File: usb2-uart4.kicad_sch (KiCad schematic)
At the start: 24 parts, among them U1 CH344Q, U13 TPNUP2202W1T2G, Y1 8MHz

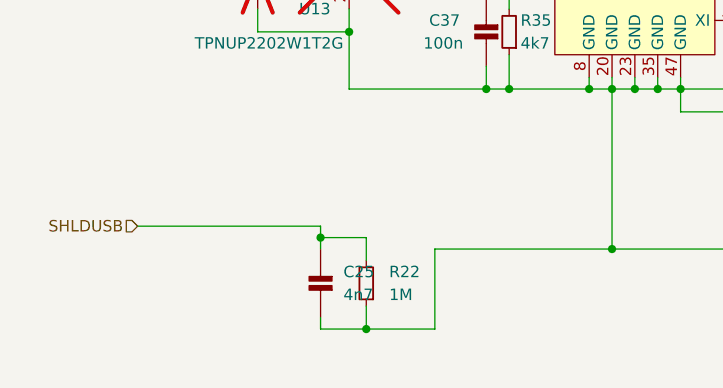
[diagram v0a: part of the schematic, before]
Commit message: Adjust R1, C1 and C10 poisitions
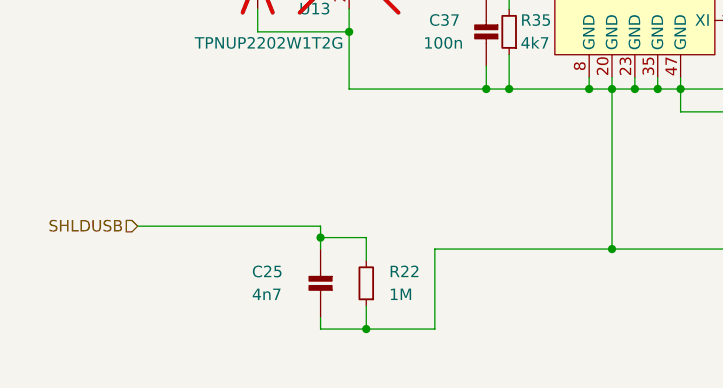
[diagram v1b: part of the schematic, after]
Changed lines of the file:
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@@
   )
   (symbol (lib_id "isouart4:CAP_NP") (at 83.82 146.05 180) (unit 1)
-    (in_bom yes) (on_board yes) (dnp no) (fields_autoplaced)
-    (property "Reference" "C25" (at 86.36 144.78 0)
+    (in_bom yes) (on_board yes) (dnp no)
+    (property "Reference" "C25" (at 76.2 144.78 0)
       (effects (font (size 1.27 1.27)) (justify right))
     )
-    (property "Value" "4n7" (at 86.36 147.32 0)
+    (property "Value" "4n7" (at 76.2 147.32 0)
       (effects (font (size 1.27 1.27)) (justify right))
     )

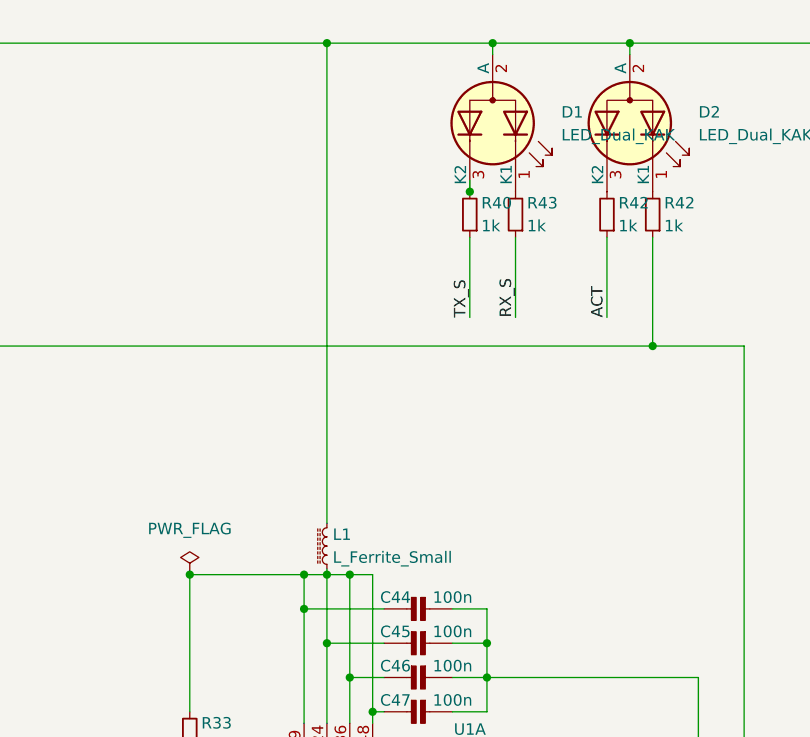
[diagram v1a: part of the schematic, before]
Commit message: adjust power filtering
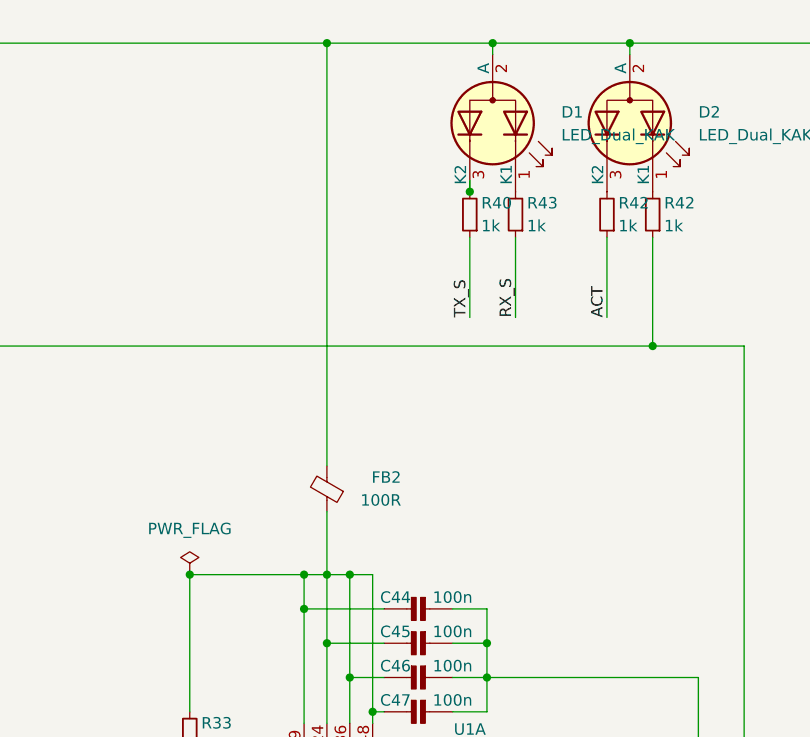
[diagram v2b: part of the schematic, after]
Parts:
- removed L1: L_Ferrite_Small, isouart4:FB_0805_2012Metric, symbol isouart4:L_Ferrite_Small
- added FB2: 100R, isouart4:FB_0805_2012Metric, symbol Device:FerriteBead_Small
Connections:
- net VIN 3.3V: now also FB2.2
- net at C44.2, C45.2, C46.2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: now also FB2.1
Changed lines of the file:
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@@
     (stroke (width 0) (type default))
   )
-  (wire (pts (xy 117.475 18.415) (xy 117.475 71.755))
+  (wire (pts (xy 117.475 18.415) (xy 117.475 65.405))
     (stroke (width 0) (type default))
   )
@@
     (stroke (width 0) (type default))
   )
-  (wire (pts (xy 117.475 76.835) (xy 117.475 77.47))
+  (wire (pts (xy 117.475 70.485) (xy 117.475 77.47))
     (stroke (width 0) (type default))
   )
@@
     )
   )
-  (symbol (lib_id "isouart4:L_Ferrite_Small") (at 117.475 74.295 180) (unit 1)
-    (in_bom yes) (on_board yes) (dnp no) (fields_autoplaced)
-    (property "Reference" "L1" (at 118.11 73.025 0)
-      (effects (font (size 1.27 1.27)) (justify right))
-    )
-    (property "Value" "L_Ferrite_Small" (at 118.11 75.565 0)
-      (effects (font (size 1.27 1.27)) (justify right))
-    )
-    (property "Footprint" "isouart4:FB_0805_2012Metric" (at 117.475 74.295 0)
-      (effects (font (size 1.27 1.27)) hide)
-    )
-    (property "Datasheet" "~" (at 117.475 74.295 0)
-      (effects (font (size 1.27 1.27)) hide)
-    )
-    (pin "1")
-    (pin "2")
-    (instances
-      (project "isouart4"
-        (path "/7c54d849-3d49-4f8e-b560-9dd1d738085c"
-          (reference "L1") (unit 1)
-        )
-        (path "/7c54d849-3d49-4f8e-b560-9dd1d738085c/2d235b8c-e233-4472-a8af-47eb53407ee3"
-          (reference "L3") (unit 1)
-        )
-      )
-    )
-  )
   (symbol (lib_id "isouart4:CAP_NP") (at 76.835 111.76 180) (unit 1)
     (in_bom no) (on_board no) (dnp yes) (fields_autoplaced)
@@
         )
       )
+    )
+  )
+  (symbol (lib_id "Device:FerriteBead_Small") (at 117.475 67.945 180) (unit 1)
+    (in_bom yes) (on_board yes) (dnp no)
+    (property "Reference" "FB2" (at 125.73 66.675 0)
+      (effects (font (size 1.27 1.27)) (justify left))
+    )
+    (property "Value" "100R" (at 125.73 69.215 0)
+      (effects (font (size 1.27 1.27)) (justify left))
+    )
+    (property "Footprint" "isouart4:FB_0805_2012Metric" (at 119.253 67.945 90)
+      (effects (font (size 1.27 1.27)) hide)
+    )
+    (property "Datasheet" "~" (at 117.475 67.945 0)
+      (effects (font (size 1.27 1.27)) hide)
+    )
+    (pin "2")
+    (pin "1")
+    (instances
+      (project "isouart4"
+        (path "/7c54d849-3d49-4f8e-b560-9dd1d738085c"
+          (reference "FB2") (unit 1)
+        )
+        (path "/7c54d849-3d49-4f8e-b560-9dd1d738085c/2d235b8c-e233-4472-a8af-47eb53407ee3"
+          (reference "FB3") (unit 1)
+        )
+      )

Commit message: Add some title text to the schematic sheets
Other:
- note added: "USB-UART"
- title: (none) -> Galvanically Isolated USB attached Quad UART
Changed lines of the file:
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@@
 (kicad_sch (version 20230121) (generator eeschema)
   (paper "A4")
+  (title_block
+    (title "Galvanically Isolated USB attached Quad UART")
+  )
   (junction (at 118.745 124.46) (diameter 0) (color 0 0 0 0)
   )
@@
     (stroke (width 0) (type default))
   )
+  (text "USB-UART" (at 182.88 176.53 0)
+    (effects (font (size 3 3) (thickness 0.6) bold) (justify left bottom))
+  )
   (label "XO" (at 131.445 109.22 0) (fields_autoplaced)

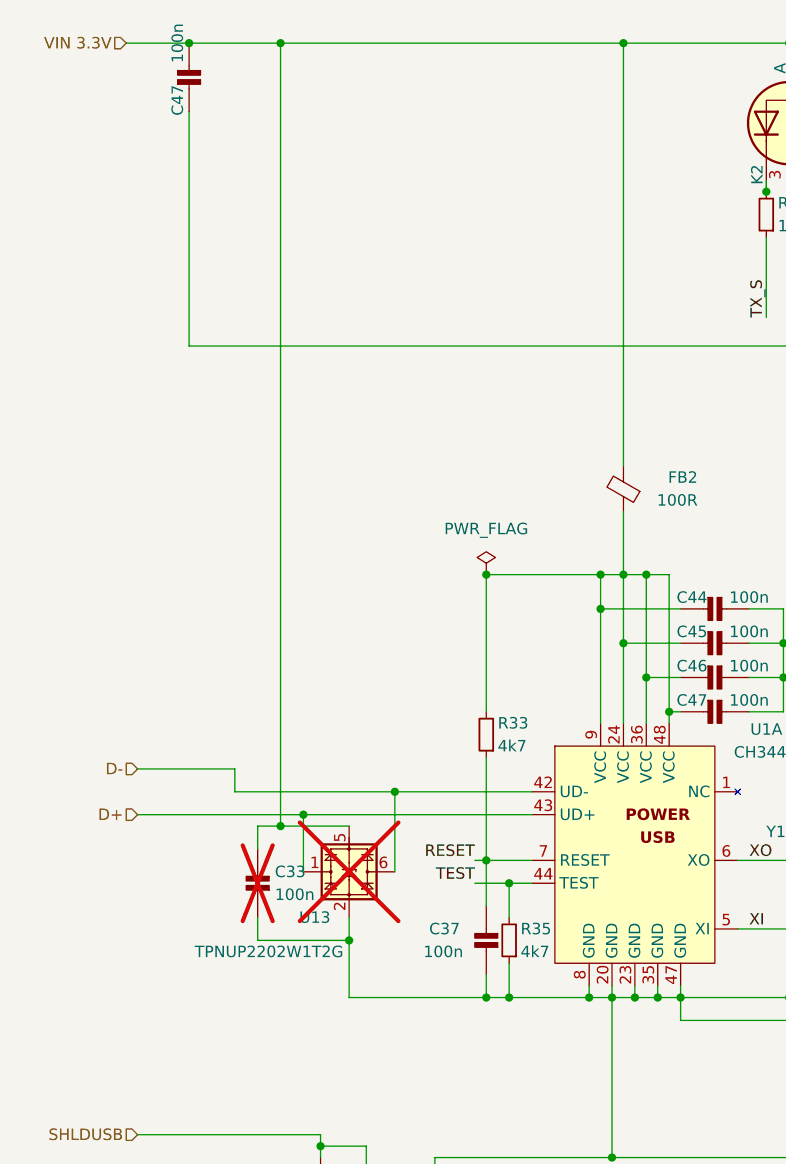
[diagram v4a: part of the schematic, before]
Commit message: rework ESD protection (handsolder sot-23 on USB connector)
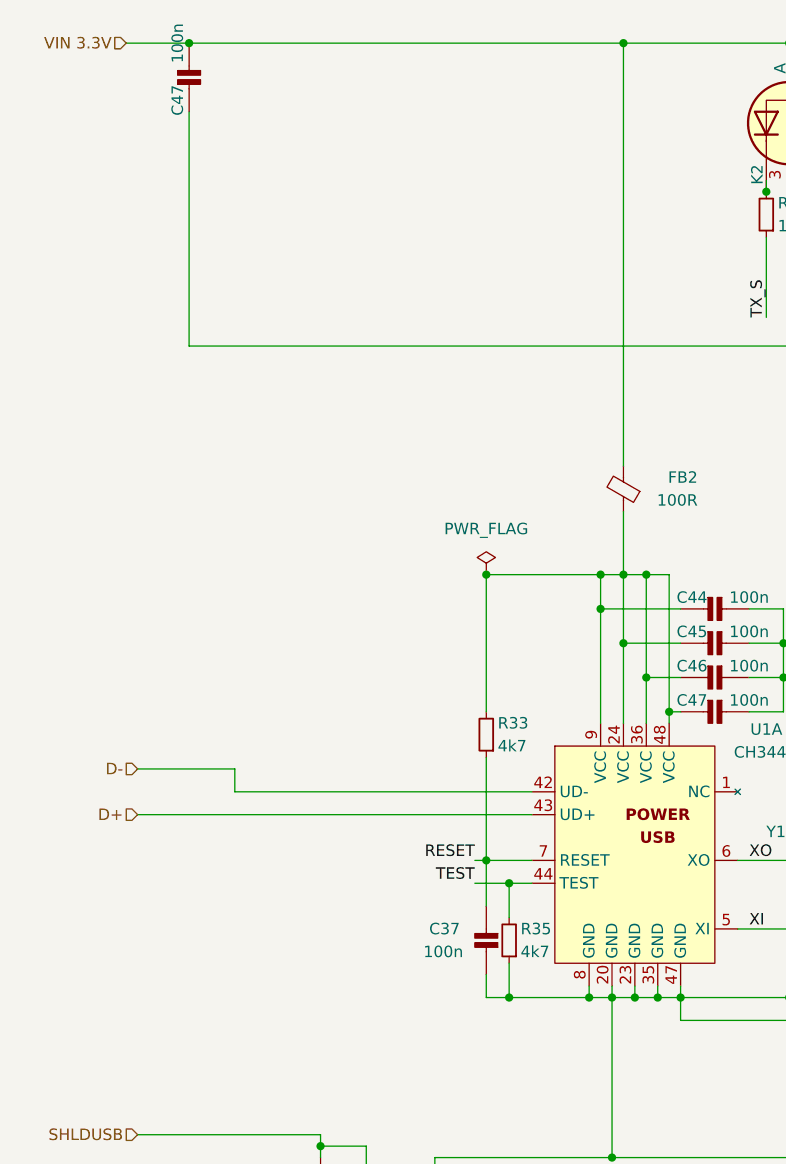
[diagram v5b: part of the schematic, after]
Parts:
- removed C33: 100n, Capacitor_SMD:C_0805_2012Metric_Pad1.18x1.45mm_HandSolder, symbol isouart4:CAP_NP
- removed U13: TPNUP2202W1T2G, Package_TO_SOT_SMD:SOT-363_SC-70-6, symbol Power_Protection:NUP2202
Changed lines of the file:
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@@
   (junction (at 135.255 85.09) (diameter 0) (color 0 0 0 0)
   )
-  (junction (at 79.375 18.415) (diameter 0) (color 0 0 0 0)
-  )
   (junction (at 114.935 77.47) (diameter 0) (color 0 0 0 0)
   )
   (junction (at 123.825 124.46) (diameter 0) (color 0 0 0 0)
   )
-  (junction (at 79.375 105.41) (diameter 0) (color 0 0 0 0)
-  )
-  (junction (at 86.995 118.11) (diameter 0) (color 0 0 0 0)
-  )
   (junction (at 153.67 52.07) (diameter 0) (color 0 0 0 0)
   )
@@
   (junction (at 117.475 18.415) (diameter 0) (color 0 0 0 0)
   )
-  (junction (at 81.915 104.14) (diameter 0) (color 0 0 0 0)
-  )
   (junction (at 139.7 109.22) (diameter 0) (color 0 0 0 0)
   )
@@
   (junction (at 121.285 124.46) (diameter 0) (color 0 0 0 0)
   )
-  (junction (at 92.075 101.6) (diameter 0) (color 0 0 0 0)
-  )
   (junction (at 104.775 111.76) (diameter 0) (color 0 0 0 0)
   )
@@
   )
   (junction (at 114.935 81.28) (diameter 0) (color 0 0 0 0)
-  )
-  (junction (at 102.235 124.46) (diameter 0) (color 0 0 0 0)
   )
   (junction (at 120.015 88.9) (diameter 0) (color 0 0 0 0)
@@
     (stroke (width 0) (type default))
   )
-  (wire (pts (xy 81.915 104.14) (xy 81.915 110.49))
-    (stroke (width 0) (type default))
-  )
   (wire (pts (xy 207.01 132.08) (xy 222.885 132.08))
     (stroke (width 0) (type default))
@@
     (stroke (width 0) (type default))
   )
-  (wire (pts (xy 69.215 18.415) (xy 79.375 18.415))
-    (stroke (width 0) (type default))
-  )
   (wire (pts (xy 207.01 96.52) (xy 227.33 96.52))
     (stroke (width 0) (type default))
@@
     (stroke (width 0) (type default))
   )
-  (wire (pts (xy 76.835 118.11) (xy 86.995 118.11))
-    (stroke (width 0) (type default))
-  )
   (wire (pts (xy 83.82 151.13) (xy 83.82 149.86))
     (stroke (width 0) (type default))
@@
     (stroke (width 0) (type default))
   )
-  (wire (pts (xy 76.835 115.57) (xy 76.835 118.11))
-    (stroke (width 0) (type default))
-  )
   (wire (pts (xy 143.51 124.46) (xy 135.89 124.46))
     (stroke (width 0) (type default))
@@
     (stroke (width 0) (type default))
   )
-  (wire (pts (xy 86.995 118.11) (xy 86.995 115.57))
-    (stroke (width 0) (type default))
-  )
   (wire (pts (xy 207.01 33.02) (xy 227.33 33.02))
     (stroke (width 0) (type default))
@@
     (stroke (width 0) (type default))
   )
-  (wire (pts (xy 79.375 105.41) (xy 76.835 105.41))
-    (stroke (width 0) (type default))
-  )
   (wire (pts (xy 139.7 116.84) (xy 144.145 116.84))
     (stroke (width 0) (type default))
@@
     (stroke (width 0) (type default))
   )
-  (wire (pts (xy 86.995 105.41) (xy 79.375 105.41))
-    (stroke (width 0) (type default))
-  )
   (wire (pts (xy 88.9 140.97) (xy 83.82 140.97))
     (stroke (width 0) (type default))
@@
     (stroke (width 0) (type default))
   )
-  (wire (pts (xy 92.075 101.6) (xy 107.315 101.6))
-    (stroke (width 0) (type default))
-  )
   (wire (pts (xy 135.255 88.9) (xy 158.75 88.9))
     (stroke (width 0) (type default))
@@
     (stroke (width 0) (type default))
   )
-  (wire (pts (xy 81.915 104.14) (xy 107.315 104.14))
-    (stroke (width 0) (type default))
-  )
-  (wire (pts (xy 76.835 105.41) (xy 76.835 107.95))
-    (stroke (width 0) (type default))
-  )
-  (wire (pts (xy 86.995 124.46) (xy 86.995 118.11))
-    (stroke (width 0) (type default))
-  )
   (wire (pts (xy 153.67 40.005) (xy 153.67 52.07))
     (stroke (width 0) (type default))
@@
     (stroke (width 0) (type default))
   )
-  (wire (pts (xy 79.375 18.415) (xy 117.475 18.415))
+  (wire (pts (xy 69.215 18.415) (xy 117.475 18.415))
     (stroke (width 0) (type default))
   )
@@
     (stroke (width 0) (type default))
   )
-  (wire (pts (xy 92.075 101.6) (xy 92.075 110.49))
-    (stroke (width 0) (type default))
-  )
-  (wire (pts (xy 63.5 104.14) (xy 81.915 104.14))
+  (wire (pts (xy 63.5 104.14) (xy 107.315 104.14))
     (stroke (width 0) (type default))
   )
@@
     (stroke (width 0) (type default))
   )
-  (wire (pts (xy 74.295 101.6) (xy 92.075 101.6))
+  (wire (pts (xy 74.295 101.6) (xy 107.315 101.6))
     (stroke (width 0) (type default))
   )
@@
     (stroke (width 0) (type default))
   )
-  (wire (pts (xy 86.995 124.46) (xy 102.235 124.46))
-    (stroke (width 0) (type default))
-  )
   (wire (pts (xy 102.235 109.22) (xy 107.315 109.22))
-    (stroke (width 0) (type default))
-  )
-  (wire (pts (xy 79.375 18.415) (xy 79.375 105.41))
     (stroke (width 0) (type default))
   )
@@
     )
   )
-  (symbol (lib_id "isouart4:CAP_NP") (at 76.835 111.76 180) (unit 1)
-    (in_bom no) (on_board no) (dnp yes) (fields_autoplaced)
-    (property "Reference" "C33" (at 78.74 110.49 0)
-      (effects (font (size 1.27 1.27)) (justify right))
-    )
-    (property "Value" "100n" (at 78.74 113.03 0)
-      (effects (font (size 1.27 1.27)) (justify right))
-    )
-    (property "Footprint" "Capacitor_SMD:C_0805_2012Metric_Pad1.18x1.45mm_HandSolder" (at 76.835 110.49 0)
-      (effects (font (size 1.27 1.27)) hide)
-    )
-    (property "Datasheet" "" (at 76.835 110.49 0)
-      (effects (font (size 1.27 1.27)) hide)
-    )
-    (property "Sim.Enable" "0" (at 76.835 111.76 0)
-      (effects (font (size 1.27 1.27)) hide)
-    )
-    (pin "1")
-    (pin "2")
-    (instances
-      (project "4WD_UART"
-        (path "/3d727dd2-df65-4f49-bc46-de00aac75be7"
-          (reference "C33") (unit 1)
-        )
-      )
-      (project "isouart4"
-        (path "/7c54d849-3d49-4f8e-b560-9dd1d738085c/2d235b8c-e233-4472-a8af-47eb53407ee3"
-          (reference "C11") (unit 1)
-        )
-      )
-    )
-  )
   (symbol (lib_id "power:PWR_FLAG") (at 102.235 77.47 0) (unit 1)
     (in_bom yes) (on_board yes) (dnp no) (fields_autoplaced)
@@
         )
       )
-    )
-  )
-  (symbol (lib_id "Power_Protection:NUP2202") (at 86.995 110.49 0) (unit 1)
-    (in_bom no) (on_board no) (dnp yes)
-    (property "Reference" "U13" (at 83.185 115.57 0)
-      (effects (font (size 1.27 1.27)))
-    )
-    (property "Value" "TPNUP2202W1T2G" (at 78.105 119.38 0)
-      (effects (font (size 1.27 1.27)))
-    )
-    (property "Footprint" "Package_TO_SOT_SMD:SOT-363_SC-70-6" (at 89.027 108.585 0)
-      (effects (font (size 1.27 1.27)) hide)
-    )
-    (property "Datasheet" "http://www.onsemi.ru.com/pub_link/Collateral/NUP2202W1-D.PDF" (at 89.027 108.585 0)
-      (effects (font (size 1.27 1.27)) hide)
-    )
-    (property "LCSC" " C2959847" (at 86.995 110.49 0)
-      (effects (font (size 1.27 1.27)) hide)
-    )
-    (property "Sim.Enable" "0" (at 86.995 110.49 0)
-      (effects (font (size 1.27 1.27)) hide)
-    )
-    (pin "1")
-    (pin "2")
-    (pin "3")
-    (pin "4")
-    (pin "5")
-    (pin "6")
-    (instances
-      (project "4WD_UART"
-        (path "/3d727dd2-df65-4f49-bc46-de00aac75be7"
-          (reference "U13") (unit 1)
-        )
-      )
-      (project "isouart4"
-        (path "/7c54d849-3d49-4f8e-b560-9dd1d738085c/2d235b8c-e233-4472-a8af-47eb53407ee3"
-          (reference "U6") (unit 1)
-        )
-      )
